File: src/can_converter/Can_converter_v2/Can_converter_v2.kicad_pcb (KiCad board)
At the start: 2 copper layers, 40.6 x 17.2 mm, 24 parts, among them J1 SM02B-PASS, J102 IDC6, U1 STM32G0B1CBT, U2 TCAN1462V, X1 629722000214_pasteInHole, Y1 830108313809

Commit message: Monkey
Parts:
- added G***: LOGO, Bluesat:Monkey, B.Cu at (130.5, 124.5)

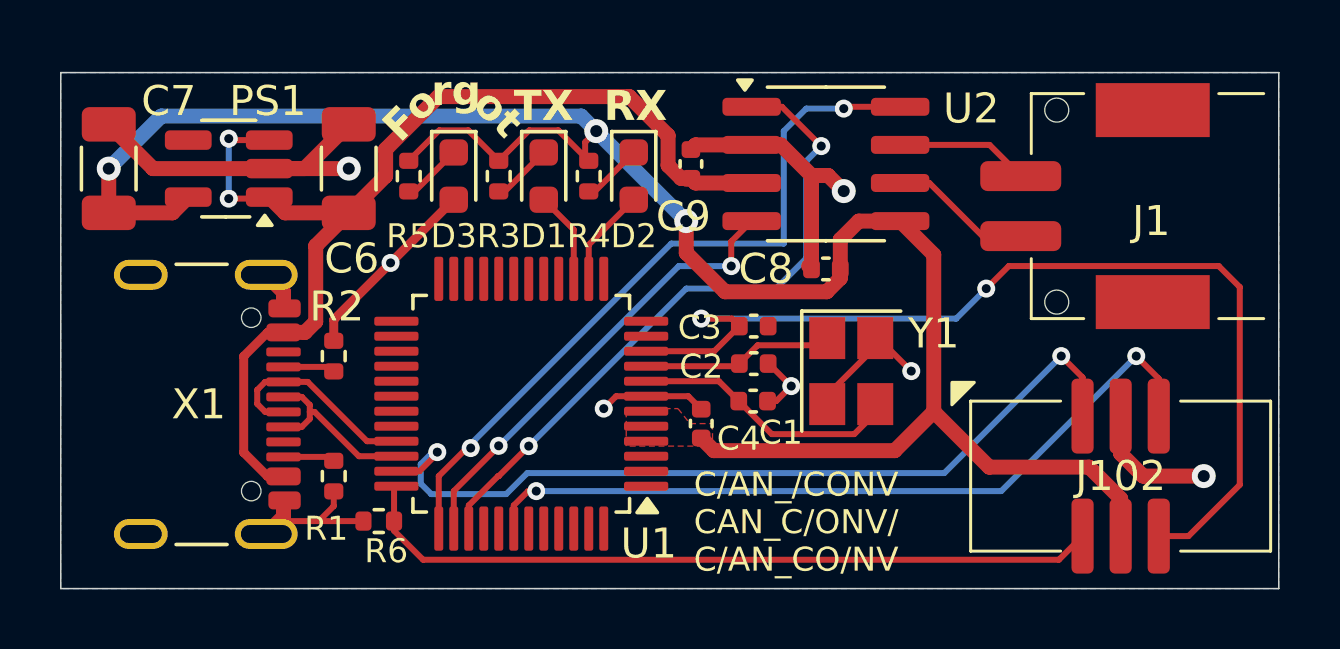
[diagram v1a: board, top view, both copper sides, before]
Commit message: Rebase usb-can branch onto main
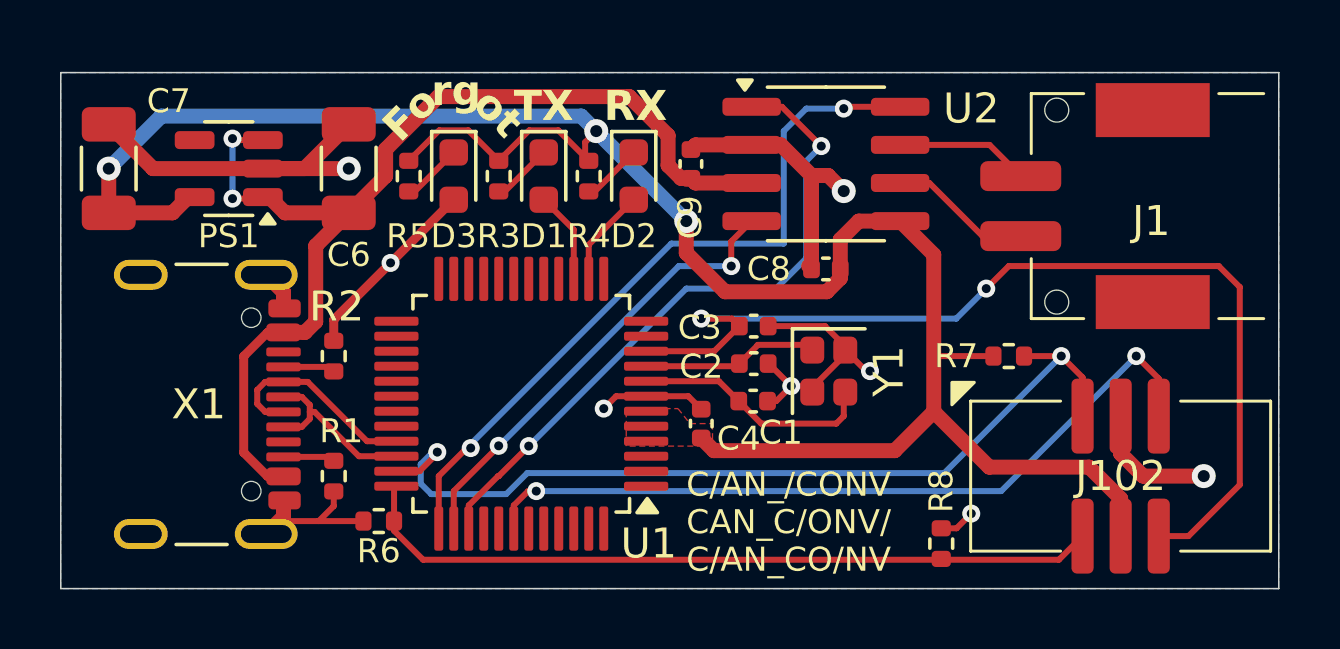
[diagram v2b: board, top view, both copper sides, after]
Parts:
- added R7: 100k, Resistor_SMD:R_0402_1005Metric, F.Cu at (142.0, 125.2)
- added R8: 100k, Resistor_SMD:R_0402_1005Metric, F.Cu at (139.8, 131.5)
- D1: value XL-1608UGC-04 -> XL-1608UYC-06
- PS1: footprint Package_TO_SOT_SMD:SOT-23-5_HandSoldering -> Package_TO_SOT_SMD:SOT-23-5
- Y1: footprint Crystal:Crystal_SMD_Abracon_ABM8AIG-4Pin_3.2x2.5mm -> Crystal:Crystal_SMD_2016-4Pin_2.0x1.6mm
- moved Y1 0.75 mm to (136.0, 125.8)
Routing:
- net GND: track 49.1 -> 52.3 mm, vias 7 -> 8
- net +3V3: track 69.1 -> 71.1 mm
- net /MCU/SWDIO: track 28.7 -> 30.0 mm
- net Net-(U1F-PF0/OSC_IN): track 8.96 -> 7.90 mm
- net Net-(U1F-PF1/OSC_OUT): track 6.43 -> 5.91 mm

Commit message: Add 100R series on crystal oscillator
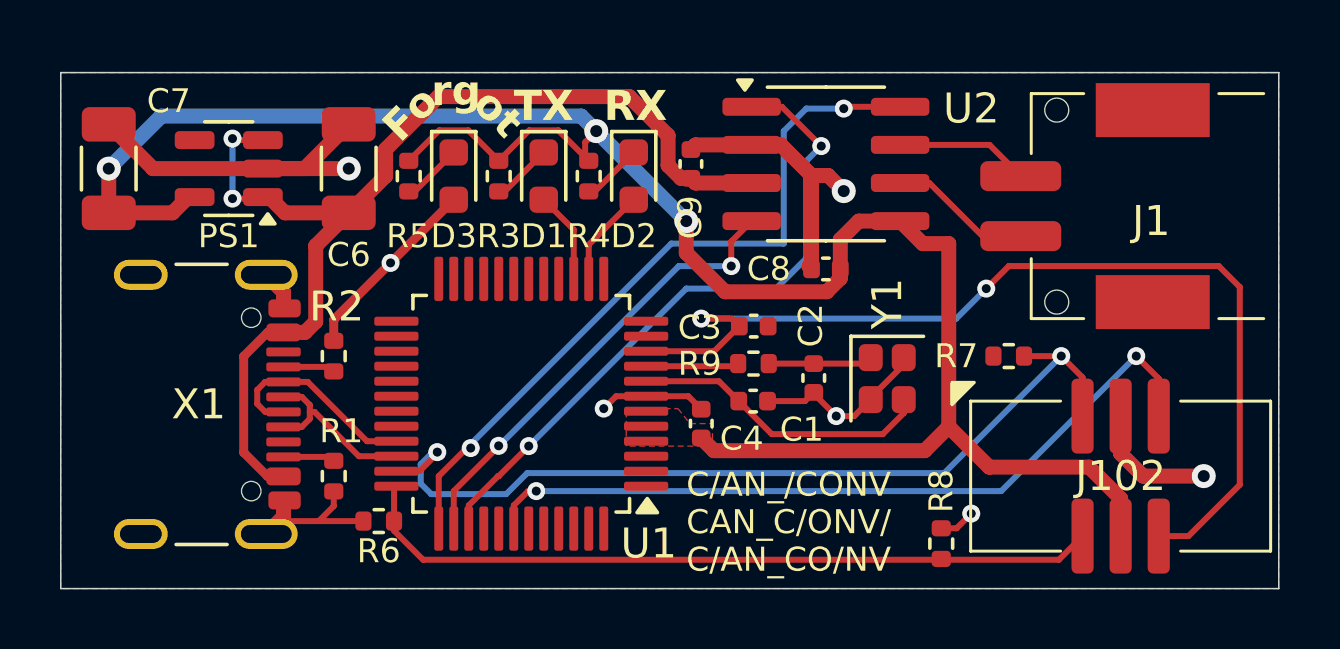
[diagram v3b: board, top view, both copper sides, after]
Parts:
- added R9: 100R, Resistor_SMD:R_0402_1005Metric, F.Cu at (133.5, 125.5)
- moved C2 2.06 mm to (135.5, 126.0), turned to 90 degrees
- moved Y1 1.97 mm to (137.9, 126.0)
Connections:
- C2 pad 2: Net-(U1F-PF1/OSC_OUT) -> Net-(Y1-C_{1})
- Y1 pad 1: Net-(U1F-PF1/OSC_OUT) -> Net-(Y1-C_{1})
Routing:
- net Net-(Y1-C_{1}): track 0.00 -> 3.48 mm
- net Net-(U1F-PF1/OSC_OUT): track 5.91 -> 3.10 mm
- net GND: track 52.3 -> 49.7 mm, vias 8 -> 7
- net Net-(U1F-PF0/OSC_IN): track 7.90 -> 10.1 mm
- net +3V3: track 71.1 -> 69.9 mm
